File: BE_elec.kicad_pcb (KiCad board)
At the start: 2 copper layers, 110 x 100 mm, 54 parts, among them J2 Conn_01x02, J3 Conn_01x03, Q1 2N2907, Q10 TIP32, Q11 BD138, Q12 TIP31, Q13 2N222, Q2 2N2907, Q3 2N2907, Q4 2N222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

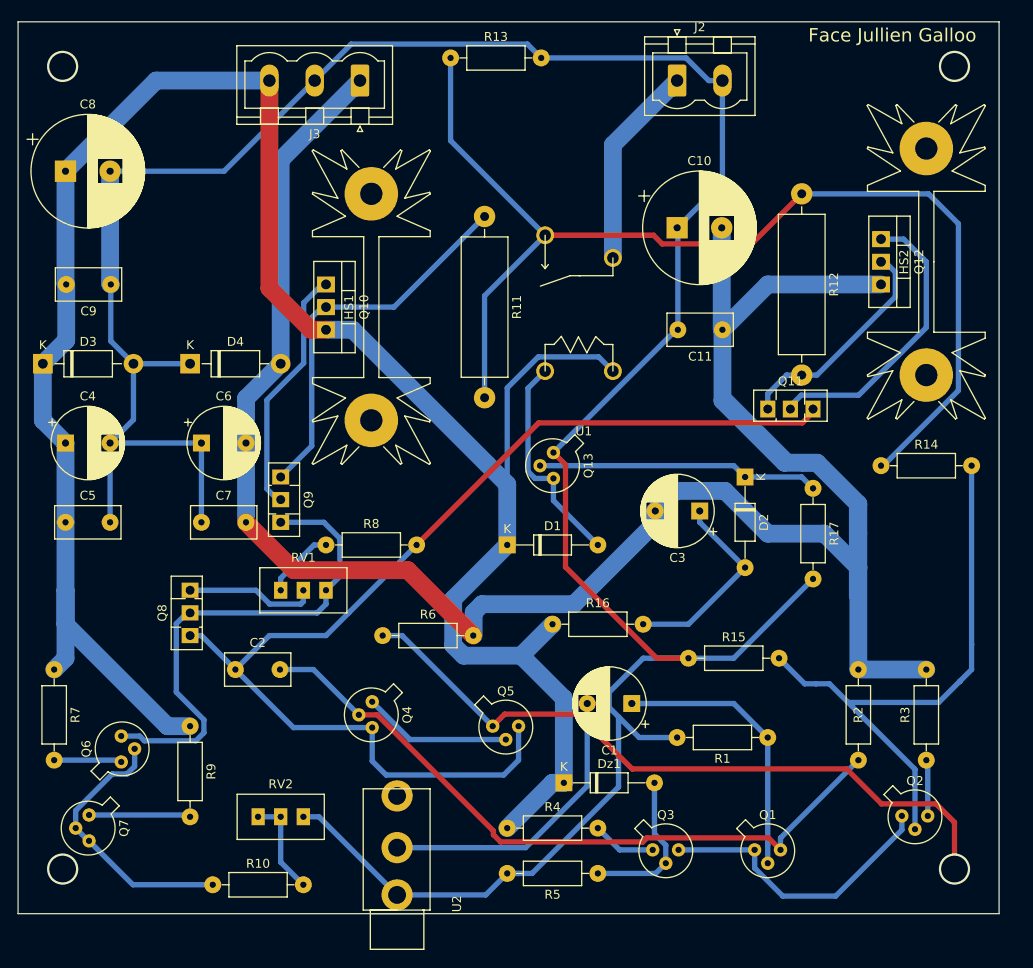
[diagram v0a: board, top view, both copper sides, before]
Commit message: bonne lib, soudures top possibles, pistes loin des pastilles, suppresion angles aigus, texte bottom en miroir, pistes larges pour les résistances de puissances, plans de masse
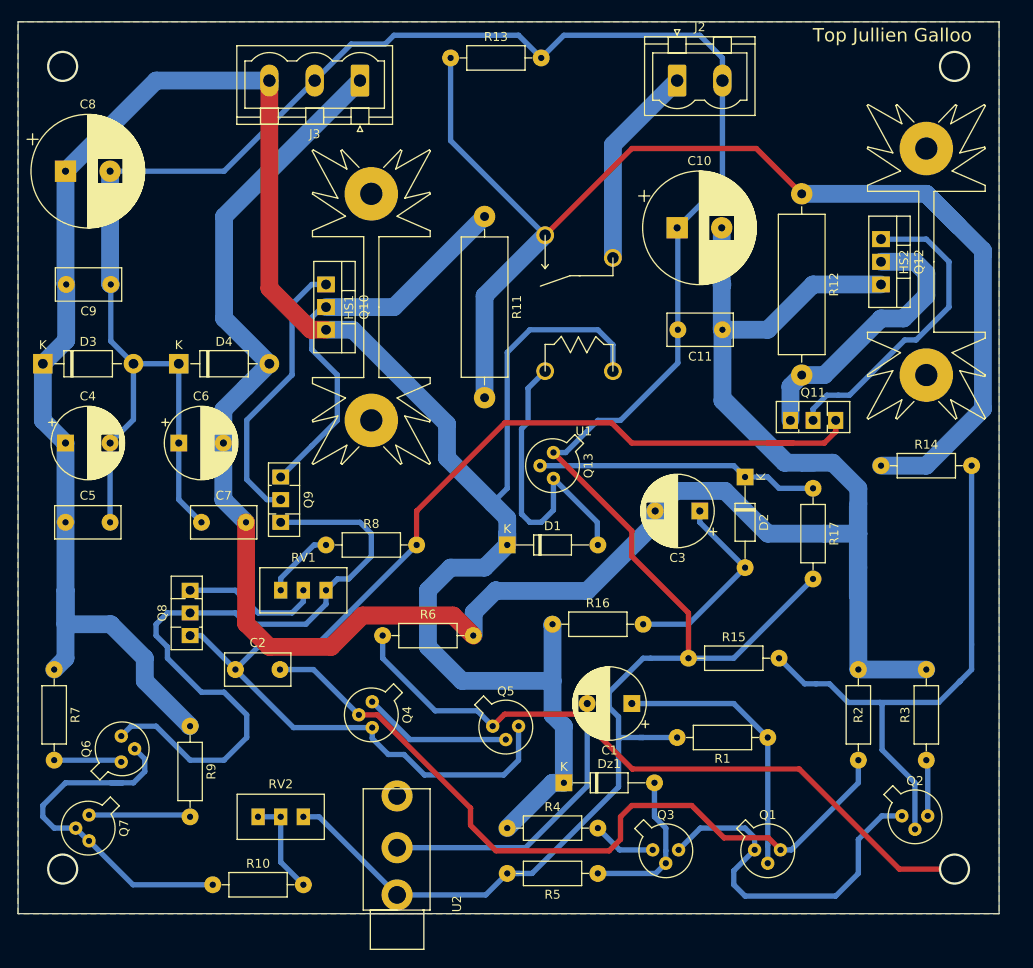
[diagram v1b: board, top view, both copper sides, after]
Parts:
- moved Q11 2.84 mm to (101.6, 59.7)
- moved C6 2.54 mm to (33.0, 62.2)
- moved D4 1.27 mm to (33.0, 53.3)
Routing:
- net Net-(Q6-Pad3): track 56.5 -> 78.0 mm
- net +12V: track 250.2 -> 270.6 mm
- net Net-(R11-Pad2): track 126.6 -> 140.5 mm
- net Net-(Q6-Pad2): track 30.6 -> 40.8 mm
- net Net-(D1-Pad2): track 24.7 -> 34.7 mm
- net -12V: track 271.9 -> 281.5 mm
- net Net-(Q1-Pad1): track 33.0 -> 41.6 mm
- net Net-(C2-Pad1): track 127.1 -> 135.1 mm
- net Net-(C2-Pad2): track 78.8 -> 85.7 mm
- net Net-(Q11-Pad1): track 25.3 -> 31.4 mm
- net Net-(Q10-Pad1): track 28.0 -> 31.3 mm
- net GND: track 316.5 -> 319.0 mm
- net Net-(Q10-Pad2): track 43.4 -> 45.8 mm
- net Net-(Q11-Pad2): track 32.7 -> 35.0 mm
- net Net-(Q5-Pad1): track 79.2 -> 77.6 mm
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- added copper zone on B.Cu, net GND
- added copper zone on F.Cu, net GND
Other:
- board text added: "Top Jullien Galloo"
- board text removed: "Face Jullien Galloo"

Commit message: bonne lib, pistes top, texte
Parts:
- C1, C3, C4, C6: footprint CmpAmpliAudio:CP_Radial_D8.0mm_P5.00mm -> TR_MaLib_Ampli_2021:CP_Radial_D8.0mm_P5.00mm
- C10, C8: footprint CmpAmpliAudio:CP_Radial_D12.5mm_P5.00mm -> TR_MaLib_Ampli_2021:CP_Radial_D12.5mm_P5.00mm
- C11, C2, C5, C7, C9: footprint CmpAmpliAudio:C_Rect_L7.2mm_W3.5mm_P5.00mm_FKS2_FKP2_MKS2_MKP2 -> TR_MaLib_Ampli_2021:C_Rect_L7.2mm_W3.5mm_P5.00mm_FKS2_FKP2_MKS2_MKP2
- D1, D2, Dz1: footprint CmpAmpliAudio:D_DO-35_SOD27_P10.16mm_Horizontal -> TR_MaLib_Ampli_2021:D_DO-35_SOD27_P10.16mm_Horizontal
- HS1, HS2: footprint CmpAmpliAudio:Heatsink_Fischer_SK104-STC-STIC_35x13mm_2xDrill2.5mm -> TR_MaLib_Ampli_2021:Heatsink_Fischer_SK104-STC-STIC_35x13mm_2xDrill2.5mm
- J2: footprint CmpAmpliAudio:PhoenixContact_MSTBVA_2,5_2-G-5,08_1x02_P5.08mm_Vertical -> TR_MaLib_Ampli_2021:PhoenixContact_MSTBVA_2,5_2-G-5,08_1x02_P5.08mm_Vertical
- J3: footprint CmpAmpliAudio:PhoenixContact_MSTBVA_2,5_3-G-5,08_1x03_P5.08mm_Vertical -> TR_MaLib_Ampli_2021:PhoenixContact_MSTBVA_2,5_3-G-5,08_1x03_P5.08mm_Vertical
- Q1, Q13, Q2, Q3, Q4, Q5, Q6, Q7: footprint CmpAmpliAudio:TO-18-3 -> TR_MaLib_Ampli_2021:TO-18-3
- Q10, Q12: footprint CmpAmpliAudio:TO-220-3_Vertical -> TR_MaLib_Ampli_2021:TO-220-3_Vertical
- Q11, Q8, Q9: footprint CmpAmpliAudio:TO-126-3_Vertical -> TR_MaLib_Ampli_2021:TO-126-3_Vertical
- R1, R10, R13, R14, R15, R16, R17, R2, R3, R4, R5, R6, R7, R8, R9: footprint CmpAmpliAudio:R_Axial_DIN0207_L6.3mm_D2.5mm_P10.16mm_Horizontal -> TR_MaLib_Ampli_2021:R_Axial_DIN0207_L6.3mm_D2.5mm_P10.16mm_Horizontal
- R11, R12: footprint CmpAmpliAudio:R_Axial_DIN0516_L15.5mm_D5.0mm_P20.32mm_Horizontal -> TR_MaLib_Ampli_2021:R_Axial_DIN0516_L15.5mm_D5.0mm_P20.32mm_Horizontal
- RV1, RV2: footprint CmpAmpliAudio:Potentiometer_Bourns_3296W_Vertical -> TR_MaLib_Ampli_2021:Potentiometer_Bourns_3296W_Vertical
- U2: footprint CmpAmpliAudio:Jack_35RAPC2AV -> TR_MaLib_Ampli_2021:Jack_35RAPC2AV
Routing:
- net Net-(C2-Pad2): track 85.7 -> 108.0 mm
- net Net-(R11-Pad2): track 140.5 -> 155.6 mm
- net -12V: track 281.5 -> 287.4 mm
- net GND: track 319.0 -> 324.8 mm
- net Net-(C2-Pad1): track 135.1 -> 140.0 mm
- net Net-(Q11-Pad2): track 35.0 -> 38.3 mm
- net Net-(Q5-Pad1): track 77.6 -> 80.3 mm
- net Net-(Q11-Pad1): track 31.4 -> 34.1 mm
- net +12V: track 270.6 -> 272.8 mm
- net Net-(D2-Pad1): track 31.7 -> 33.2 mm
- net Net-(Q1-Pad1): track 41.6 -> 43.0 mm

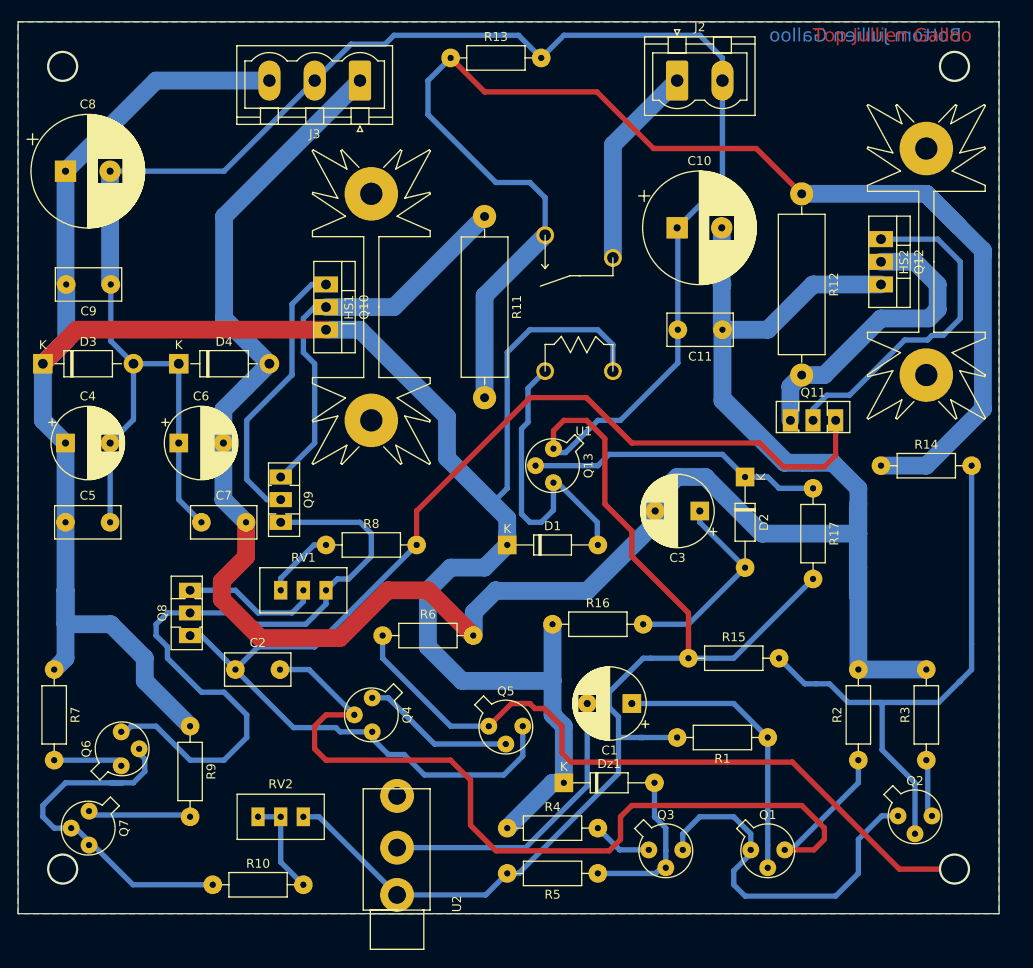
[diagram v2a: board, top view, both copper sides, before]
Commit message: Amélioration routage top, direct bornier-->TIP
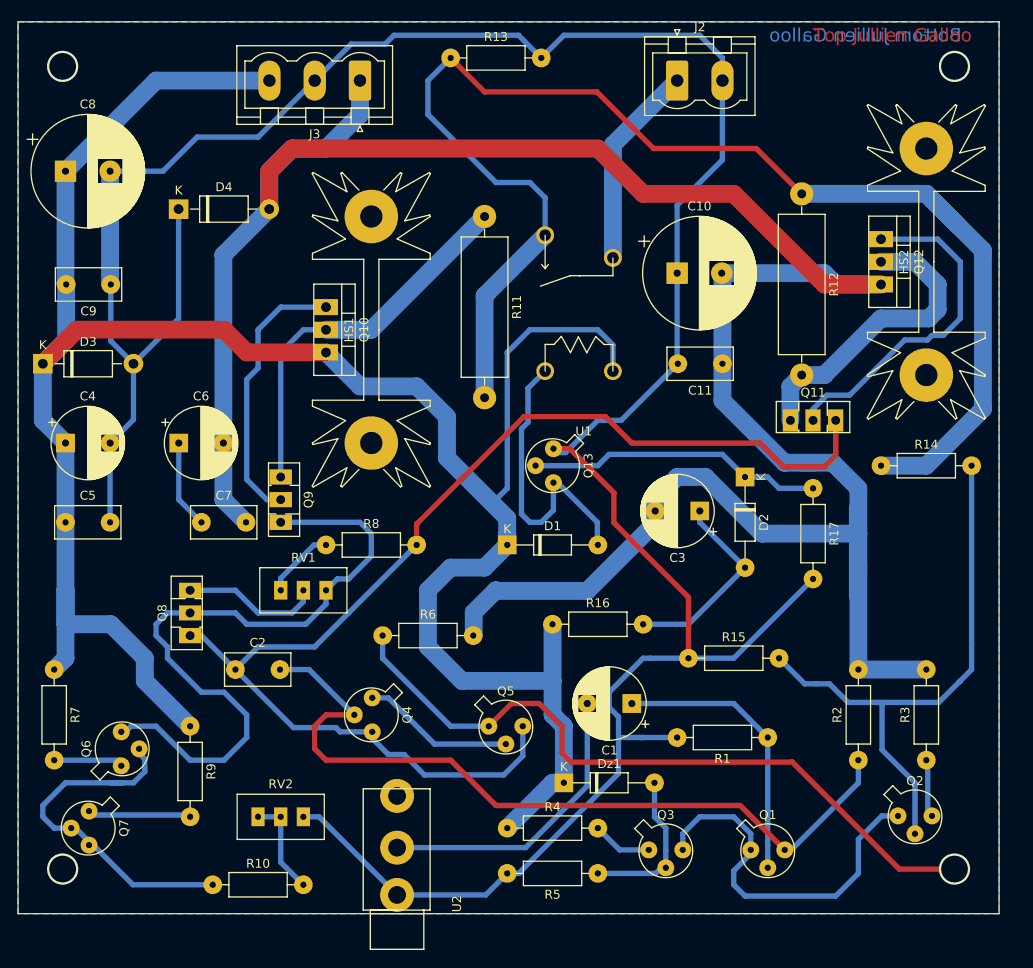
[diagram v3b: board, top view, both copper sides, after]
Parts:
- moved D4 17.3 mm to (33.0, 36.0)
- moved C10 5.08 mm to (88.9, 43.2)
- moved C11 3.81 mm to (94.0, 53.3)
- moved HS1 2.54 mm to (54.6, 49.5)
- moved Q10 2.54 mm to (49.5, 47.0)
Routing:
- net Net-(C2-Pad2): track 108.0 -> 89.7 mm
- net -12V: track 287.4 -> 297.6 mm
- net Net-(C2-Pad1): track 140.0 -> 137.4 mm
- net Net-(Q10-Pad2): track 45.4 -> 43.1 mm
- net GND: track 324.8 -> 323.5 mm
- net Net-(Q10-Pad1): track 31.3 -> 32.4 mm
